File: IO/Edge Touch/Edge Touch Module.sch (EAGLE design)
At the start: 3 parts

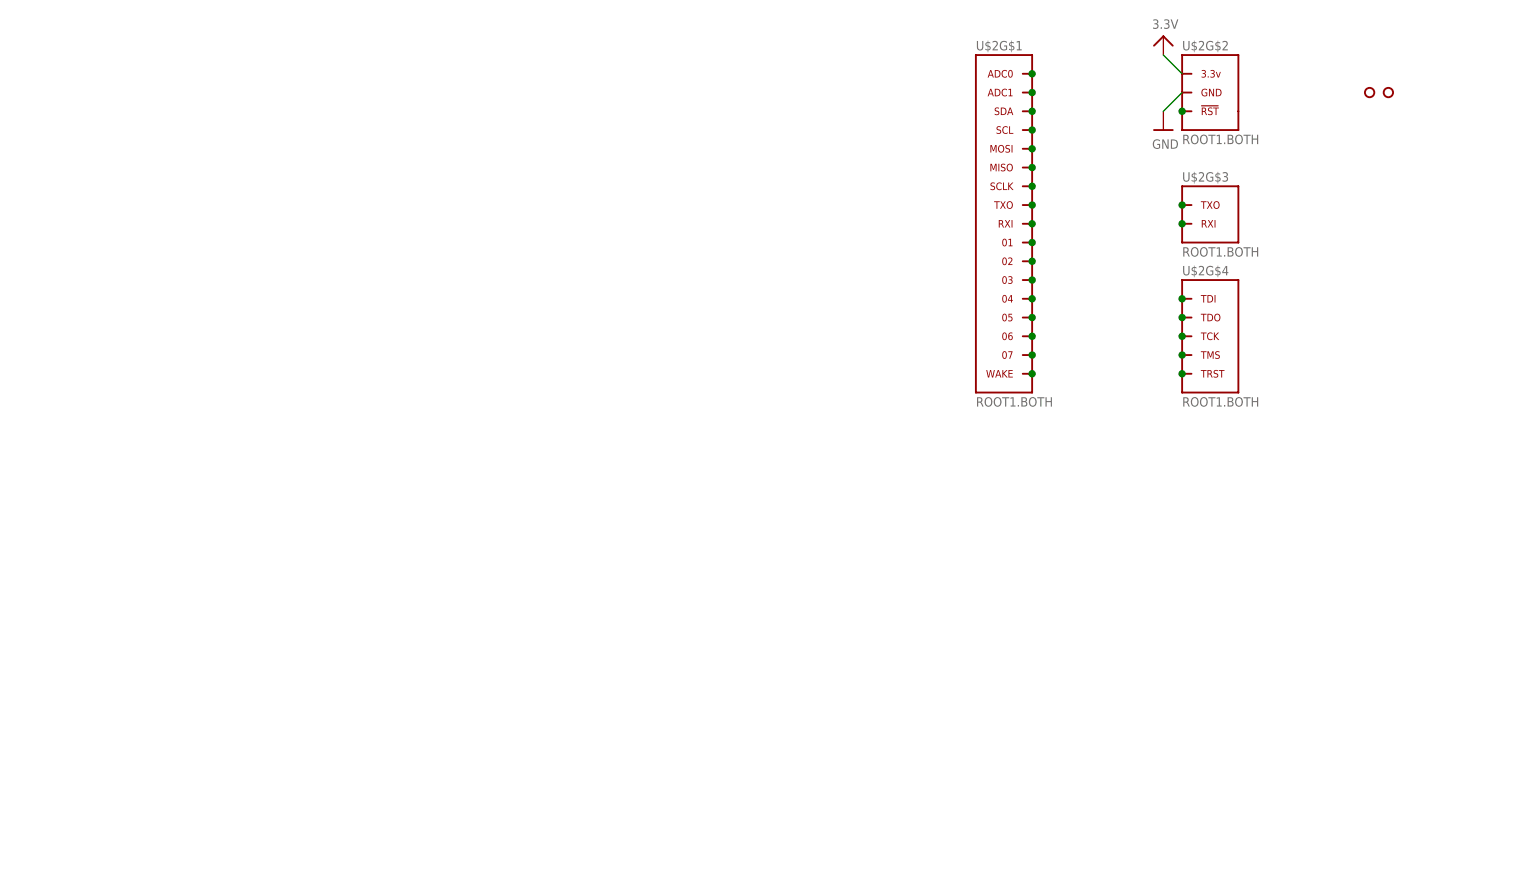
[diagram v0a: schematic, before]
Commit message: Created and completed Edge Touch Module
Signed-off-by: Cruz Monrreal II <Cruz.Monrreal@gmail.com>
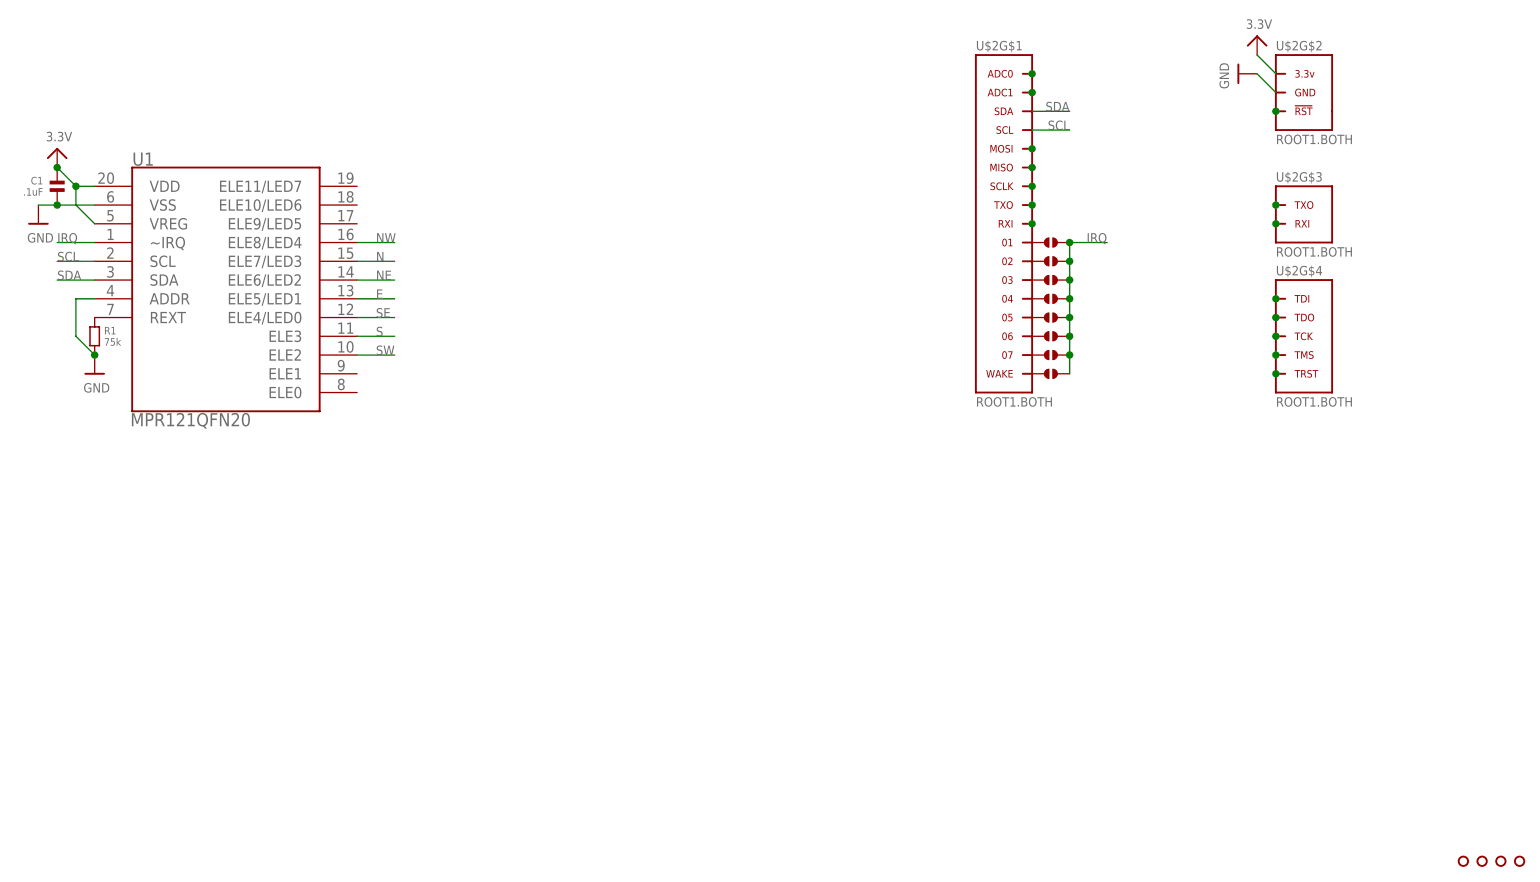
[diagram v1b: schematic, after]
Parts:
- added 1, 8, J2, J3, J4, J5, J6, J7: (no value), .solderjumper:SOLDERJUMPER.2.SML
- added C1: .1uF, .standardparts:CAPACITOR.0603
- added R1: 75k, .standardparts:RESISTOR.0603
- added U$10, U$9: HOLE.#2, .screw_holes:HOLE.#2
- added U1: MPR121QFN20, SparkFun-Sensors:MPR121QFN20
- U$3, U$4: value HOLE.2MM -> HOLE.#2; device .screw_holes:HOLE.2MM -> .screw_holes:HOLE.#2
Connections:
- removed net N$17: U$2G$1.WAKE
- removed net N$4: U$2G$1.SCL
- new net E: U1.ELE5/LED1
- new net IRQ: 1.2, 8.2, J2.2, J3.2, J4.2, J5.2, J6.2, J7.2, U1.~IRQ
- new net N: U1.ELE7/LED3
- new net N$26: R1.1, U1.REXT
- new net NE: U1.ELE6/LED2
- new net NW: U1.ELE8/LED4
- new net S: U1.ELE3
- new net SCL: U$2G$1.SCL, U1.SCL
- new net SDA: U$2G$1.SDA, U1.SDA
- new net SE: U1.ELE4/LED0
- new net SW: U1.ELE2
- net 3.3V: now also C1.1, U1.VDD, U1.VREG
- net GND: now also C1.2, R1.2, U1.ADDR, U1.VSS
- net N$1: now also 1.1, U$2G$1.01; no longer U$2G$1.04
- net N$10: now also J4.1, U$2G$1.04; no longer U$2G$1.01
- net N$11: now also J5.1, U$2G$1.05; no longer U$2G$1.02
- net N$14: now also J6.1, U$2G$1.06; no longer U$2G$1.05
- net N$15: now also J7.1, U$2G$1.07; no longer U$2G$1.06
- net N$16: now also 8.1, U$2G$1.WAKE; no longer U$2G$1.07
- net N$3: now also J2.1, U$2G$1.02; no longer U$2G$1.SDA
- net N$5: now also J3.1
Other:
- moved on the sheet: U$2G$2, U$2G$3, U$2G$4
